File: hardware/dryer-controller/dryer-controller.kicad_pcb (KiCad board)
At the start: 2 copper layers, 110 x 85 mm, 69 parts, among them K1 SRD-05VDC-SL-C, K2 SRD-05VDC-SL-C, Q1 MMBT2222A, Q2 MMBT2222A, Q3 CJ2310, Q4 CJ2310, Q5 CJ2310, SW1 SW-USB, U1 K7805-1000R3

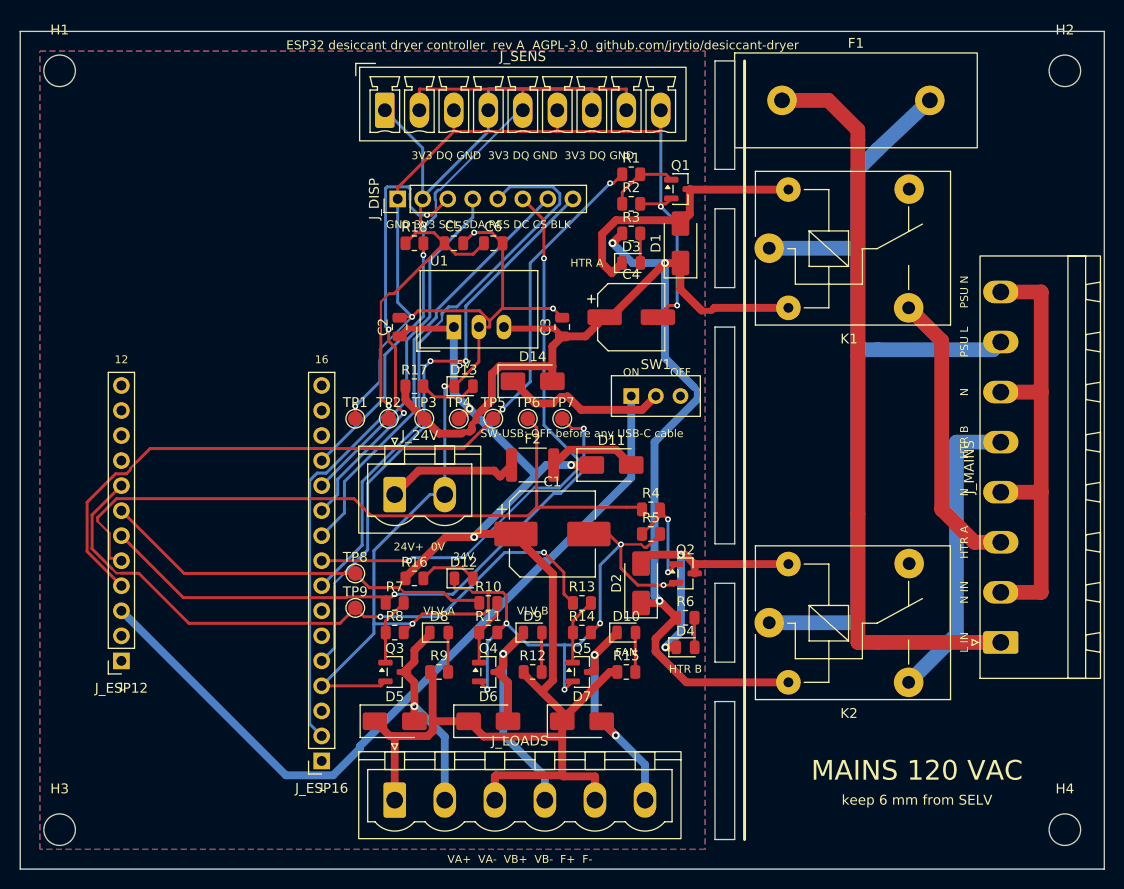
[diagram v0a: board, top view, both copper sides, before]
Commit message: Keep tracks and vias out from under the 5 V converter
TRACO's TSR-1 datasheet says not to route under the converter; the
routed board had 34 track segments inside U1's courtyard. A new
u1_keepout rule area (both copper layers, tracks and vias forbidden,
pours and pads allowed) covers the courtyard from its top to y 29.5.
Down to y 30, the pad row's centre line, the router left nine
connections unrouted (U1 pads 1 and 3 among them), so it stops 0.5 mm
short, the fallback the review allowed.

With the area in place Freerouting necked a GND track to 0.18 mm, under
the 0.2 mm minimum, to pass R17's pad; R17 moves 0.5 mm down to y 36.5
and the route is clean. Re-routed with 200 passes: DRC 0 violations, 0
unconnected, no track or via inside the area on either layer (a new
routed-board test checks the exact copper outline). check_sync and the
board test expect the new area.

Co-Authored-By: Claude Opus 5.5 <noreply@anthropic.com>
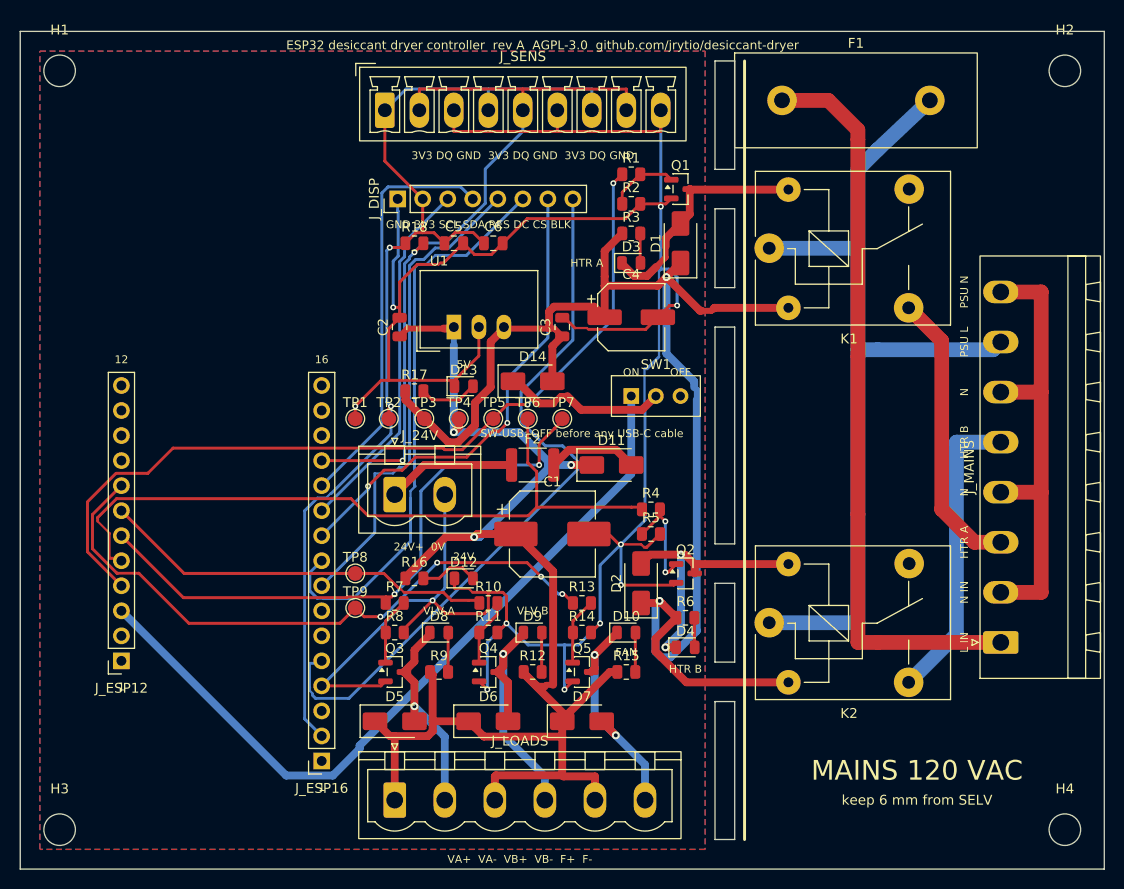
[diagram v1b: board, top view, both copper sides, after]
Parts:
- moved R17 0.50 mm to (40.0, 36.5)
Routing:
- net GND: track 250.2 -> 275.6 mm, vias 14 -> 11
- net LCD_BL: track 59.5 -> 74.7 mm, vias 2 -> 0
- net +5V: track 132.4 -> 144.2 mm, vias 3 -> 2
- net SPI_CLK: track 46.2 -> 36.9 mm, vias 3 -> 0
- net LCD_RST: track 57.4 -> 49.4 mm
- net SPI_MOSI: track 35.4 -> 42.2 mm
- net +24V: track 139.7 -> 145.8 mm
- net OW_DQ: track 73.1 -> 78.9 mm, vias 1 -> 2
- net COIL_A: track 28.4 -> 23.8 mm
- net LCD_CS: track 43.7 -> 48.3 mm, vias 0 -> 2
- net FAN: track 66.7 -> 64.5 mm, vias 2 -> 4
- net +3V3: track 109.4 -> 107.8 mm, vias 1 -> 2
- net LCD_DC: track 59.8 -> 58.4 mm, vias 2 -> 0
- net HTR_A: track 85.1 -> 86.2 mm
- net VLV_A: track 62.3 -> 61.4 mm
